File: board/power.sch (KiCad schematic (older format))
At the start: 38 parts, among them U201 ADP3334, U202 ADP3334, U203 LP2985

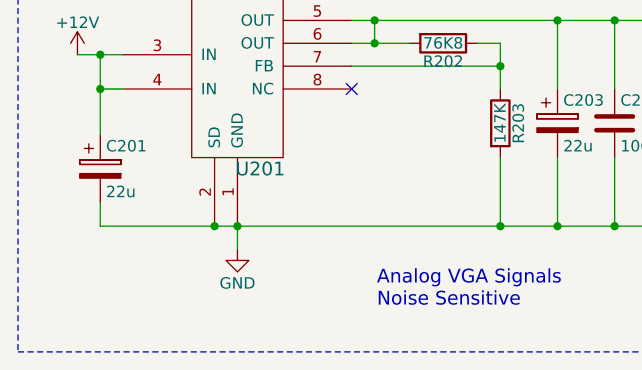
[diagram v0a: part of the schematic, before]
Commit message: Updating netlist.
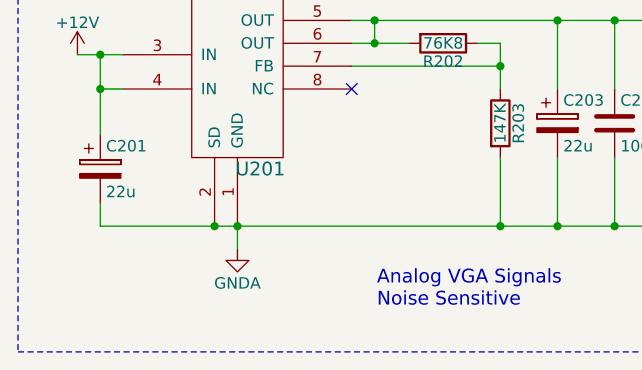
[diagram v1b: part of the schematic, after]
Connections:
- net GND: no longer C201.2, C203.2, C205.2, C207.2, C209.2, C211.2, C213.2, R203.2, R205.2, U201.1 (GND), U201.2 (SD)
- new net GNDA: C201.2, C203.2, C205.2, C207.2, C209.2, C211.2, C213.2, R203.2, R205.2, U201.1 (GND), U201.2 (SD)
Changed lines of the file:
@@
 Connection ~ 2900 4300
 $Comp
-L GND #PWR02
+L GNDA #PWR02
 U 1 1 563F0C8E
 P 2300 5300
 F 0 "#PWR02" H 2300 5050 50  0001 C CNN
-F 1 "GND" H 2300 5150 50  0000 C CNN
+F 1 "GNDA" H 2300 5150 50  0000 C CNN
 F 2 "" H 2300 5300 60  0000 C CNN
 F 3 "" H 2300 5300 60  0000 C CNN

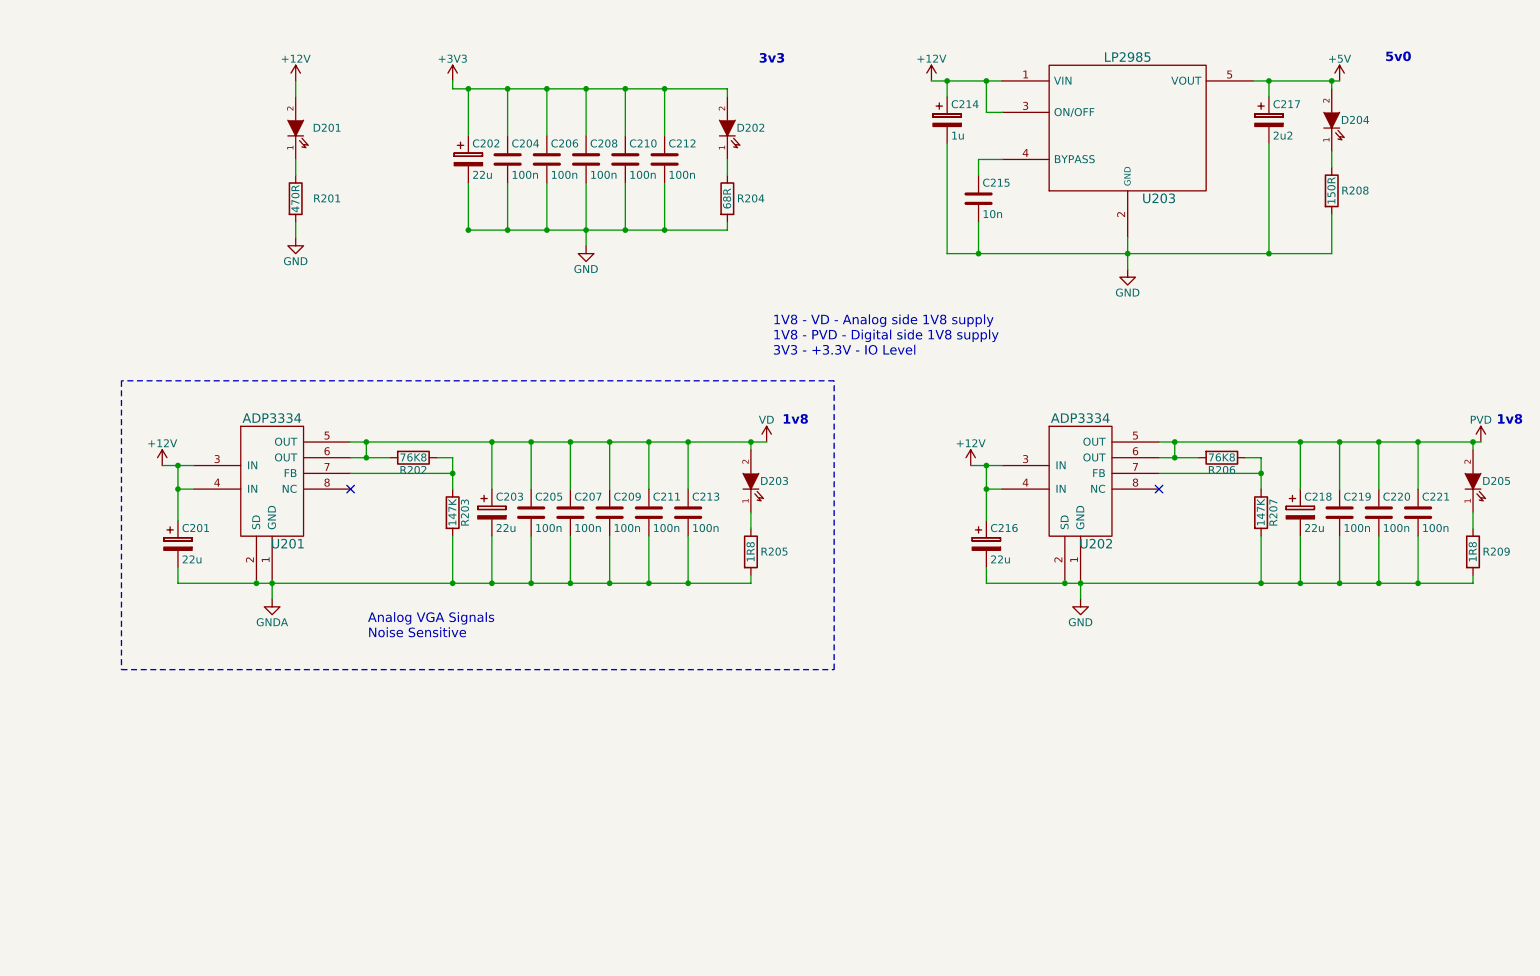
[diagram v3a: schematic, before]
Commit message: Lots of small tweaks.
 * Giving things better reference names.
 * Giving a bunch of nets names.
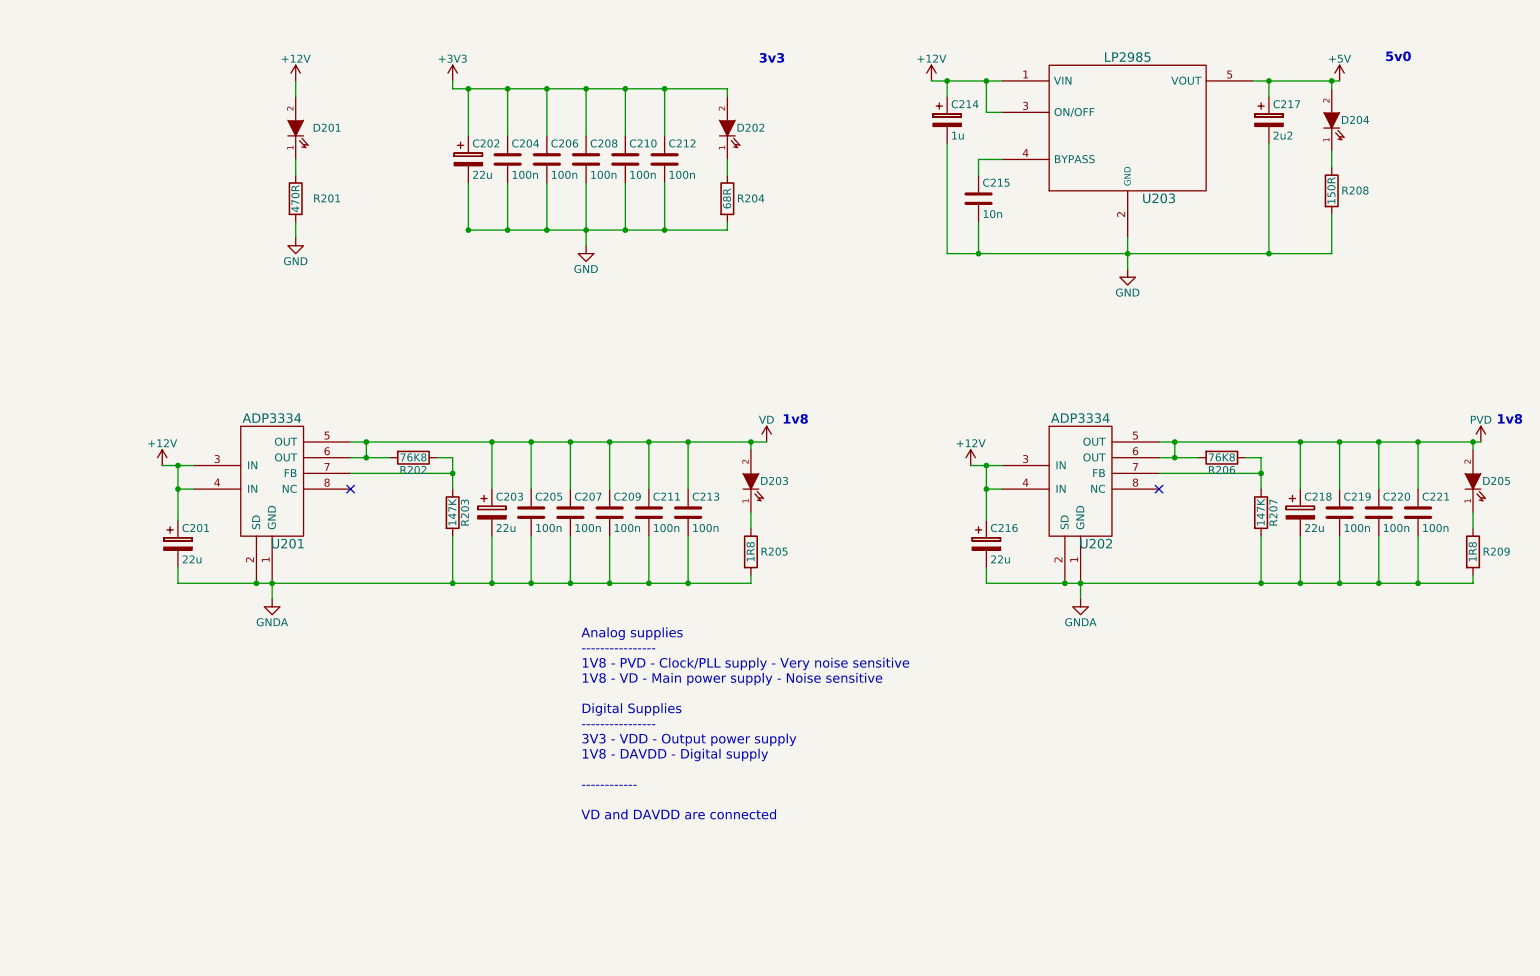
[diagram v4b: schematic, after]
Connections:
- net GND: no longer C216.2, C218.2, C219.2, C220.2, C221.2, R207.2, R209.2, U202.1 (GND), U202.2 (SD)
- net GNDA: now also C216.2, C218.2, C219.2, C220.2, C221.2, R207.2, R209.2, U202.1 (GND), U202.2 (SD)
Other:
- note added: "Analog supplies\n----------------\n1V8 - PVD - Clock/PLL supply - Very noise sensitive\n1V8 - VD - Main power supply - Noise sensitive\n\nDigital Supplies\n----------------\n3V3 - VDD - Output power supply\n1V8 - DAVDD - Digital supply\n\n------------\n\nVD and DAVDD are connected"
- note removed: "1V8 - VD - Analog side 1V8 supply\n1V8 - PVD - Digital side 1V8 supply\n3V3 - +3.3V - IO Level"
- note removed: "Analog VGA Signals\nNoise Sensitive\n"
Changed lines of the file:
@@
 Connection ~ 8050 4300
 $Comp
-L GND #PWR11
+L GNDA #PWR11
 U 1 1 56420FD1
 P 7450 5300
 F 0 "#PWR11" H 7450 5050 50  0001 C CNN
-F 1 "GND" H 7450 5150 50  0000 C CNN
+F 1 "GNDA" H 7450 5150 50  0000 C CNN
 F 2 "" H 7450 5300 60  0000 C CNN
 F 3 "" H 7450 5300 60  0000 C CNN
@@
 Text Notes 9390 1890 0    60   ~ 12
 5v0
-Text Notes 5490 3760 0    60   ~ 0
-1V8 - VD - Analog side 1V8 supply\n1V8 - PVD - Digital side 1V8 supply\n3V3 - +3.3V - IO Level
-Text Notes 2910 5560 0    60   ~ 0
-Analog VGA Signals\nNoise Sensitive\n
-Wire Notes Line
-	1340 3910 1340 5750
-Wire Notes Line
-	1340 5750 5880 5750
-Wire Notes Line
-	5880 5750 5880 3910
-Wire Notes Line
-	5880 3910 1340 3910
+Text Notes 4270 6720 0    60   ~ 0
+Analog supplies\n----------------\n1V8 - PVD - Clock/PLL supply - Very noise sensitive\n1V8 - VD - Main power supply - Noise sensitive\n\nDigital Supplies\n----------------\n3V3 - VDD - Output power supply\n1V8 - DAVDD - Digital supply\n\n------------\n\nVD and DAVDD are connected
 $EndSCHEMATC

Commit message: More and hopefully better labelling.
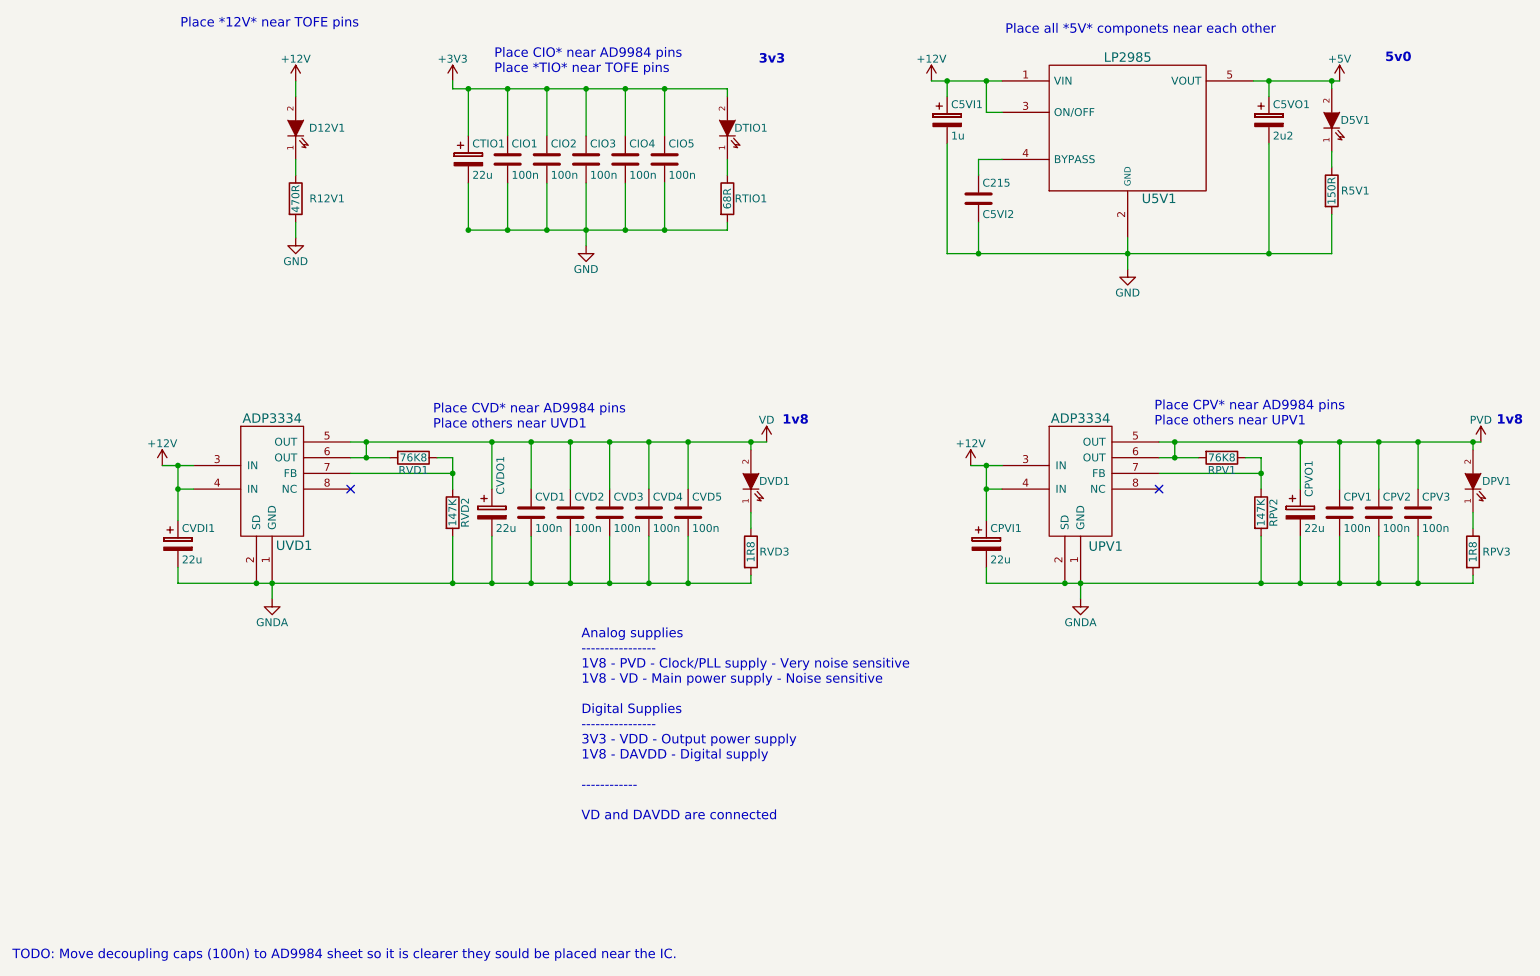
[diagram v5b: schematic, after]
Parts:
- C215: value 10n -> C5VI2
- renumbered C214 to C5VI1, C217 to C5VO1, C204 to CIO1, C206 to CIO2, C208 to CIO3, C210 to CIO4, C212 to CIO5, C219 to CPV1, C220 to CPV2, C221 to CPV3, C216 to CPVI1, C218 to CPVO1, C202 to CTIO1, C205 to CVD1, C207 to CVD2, C209 to CVD3, C211 to CVD4, C213 to CVD5, C201 to CVDI1, C203 to CVDO1, D201 to D12V1, D204 to D5V1, D205 to DPV1, D202 to DTIO1, D203 to DVD1, R201 to R12V1, R208 to R5V1, R206 to RPV1, R207 to RPV2, R209 to RPV3, R204 to RTIO1, R202 to RVD1, R203 to RVD2, R205 to RVD3, U203 to U5V1, U202 to UPV1, U201 to UVD1
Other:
- note added: "Place *12V* near TOFE pins"
- note added: "Place CIO* near AD9984 pins\nPlace *TIO* near TOFE pins"
- note added: "Place CPV* near AD9984 pins\nPlace others near UPV1"
- note added: "Place CVD* near AD9984 pins\nPlace others near UVD1"
- note added: "Place all *5V* componets near each other"
- note added: "TODO: Move decoupling caps (100n) to AD9984 sheet so it is clearer they sould be placed near the IC."

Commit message: Updating net names.
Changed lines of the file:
@@
 $EndDescr
 $Comp
-L GND #PWR02
+L GND #PWR7
 U 1 1 563EFCF4
 P 4300 3050
-F 0 "#PWR02" H 4300 2800 50  0001 C CNN
+F 0 "#PWR7" H 4300 2800 50  0001 C CNN
 F 1 "GND" H 4300 2900 50  0000 C CNN
 F 2 "" H 4300 3050 60  0000 C CNN
@@
 Connection ~ 2900 4300
 $Comp
-L GNDA #PWR03
+L GNDA #PWR3
 U 1 1 563F0C8E
 P 2300 5300
-F 0 "#PWR03" H 2300 5050 50  0001 C CNN
+F 0 "#PWR3" H 2300 5050 50  0001 C CNN
 F 1 "GNDA" H 2300 5150 50  0000 C CNN
 F 2 "" H 2300 5300 60  0000 C CNN
@@
 	2300 5200 2300 5300
 $Comp
-L PVD #PWR04
+L PVD #PWR14
 U 1 1 56411BE9
 P 10000 4300
-F 0 "#PWR04" H 10000 4150 50  0001 C CNN
+F 0 "#PWR14" H 10000 4150 50  0001 C CNN
 F 1 "PVD" H 10000 4440 50  0000 C CNN
 F 2 "" H 10000 4300 60  0000 C CNN
@@
 $EndComp
 $Comp
-L VD #PWR05
+L VD #PWR8
 U 1 1 56411CB5
 P 5450 4300
-F 0 "#PWR05" H 5450 4150 50  0001 C CNN
+F 0 "#PWR8" H 5450 4150 50  0001 C CNN
 F 1 "VD" H 5450 4440 50  0000 C CNN
 F 2 "" H 5450 4300 60  0000 C CNN
@@
 Connection ~ 8050 4300
 $Comp
-L GNDA #PWR06
+L GNDA #PWR11
 U 1 1 56420FD1
 P 7450 5300
-F 0 "#PWR06" H 7450 5050 50  0001 C CNN
+F 0 "#PWR11" H 7450 5050 50  0001 C CNN
 F 1 "GNDA" H 7450 5150 50  0000 C CNN
 F 2 "" H 7450 5300 60  0000 C CNN
@@
 	6850 5200 9950 5200
 $Comp
-L +5V #PWR07
+L +5V #PWR13
 U 1 1 5642563F
 P 9100 2000
-F 0 "#PWR07" H 9100 1850 50  0001 C CNN
+F 0 "#PWR13" H 9100 1850 50  0001 C CNN
 F 1 "+5V" H 9100 2140 50  0000 C CNN
 F 2 "" H 9100 2000 60  0000 C CNN
@@
 $EndComp
 $Comp
-L +12V #PWR08
+L +12V #PWR9
 U 1 1 56426036
 P 6500 2000
-F 0 "#PWR08" H 6500 1850 50  0001 C CNN
+F 0 "#PWR9" H 6500 1850 50  0001 C CNN
 F 1 "+12V" H 6500 2140 50  0000 C CNN
 F 2 "" H 6500 2000 60  0000 C CNN
@@
 Connection ~ 6800 3100
 $Comp
-L GND #PWR09
+L GND #PWR12
 U 1 1 56426AF7
 P 7750 3200
-F 0 "#PWR09" H 7750 2950 50  0001 C CNN
+F 0 "#PWR12" H 7750 2950 50  0001 C CNN
 F 1 "GND" H 7750 3050 50  0000 C CNN
 F 2 "" H 7750 3200 60  0000 C CNN
@@
 $EndComp
 $Comp
-L +12V #PWR010
+L +12V #PWR10
 U 1 1 5642782E
 P 6750 4450
-F 0 "#PWR010" H 6750 4300 50  0001 C CNN
+F 0 "#PWR10" H 6750 4300 50  0001 C CNN
 F 1 "+12V" H 6750 4590 50  0000 C CNN
 F 2 "" H 6750 4450 60  0000 C CNN
@@
 $EndComp
 $Comp
-L +12V #PWR011
+L +12V #PWR2
 U 1 1 5642787C
 P 1600 4450
-F 0 "#PWR011" H 1600 4300 50  0001 C CNN
+F 0 "#PWR2" H 1600 4300 50  0001 C CNN
 F 1 "+12V" H 1600 4590 50  0000 C CNN
 F 2 "" H 1600 4450 60  0000 C CNN
@@
 $EndComp
 $Comp
-L +3V3 #PWR012
+L +3V3 #PWR6
 U 1 1 56924AD1
 P 3450 2000
-F 0 "#PWR012" H 3450 1850 50  0001 C CNN
+F 0 "#PWR6" H 3450 1850 50  0001 C CNN
 F 1 "+3V3" H 3450 2140 50  0000 C CNN
 F 2 "" H 3450 2000 50  0000 C CNN
@@
 $EndComp
 $Comp
-L +12V #PWR013
+L +12V #PWR4
 U 1 1 56924BE7
 P 2450 2000
-F 0 "#PWR013" H 2450 1850 50  0001 C CNN
+F 0 "#PWR4" H 2450 1850 50  0001 C CNN
 F 1 "+12V" H 2450 2140 50  0000 C CNN
 F 2 "" H 2450 2000 50  0000 C CNN
@@
 $EndComp
 $Comp
-L GND #PWR014
+L GND #PWR5
 U 1 1 56925059
 P 2450 3000
-F 0 "#PWR014" H 2450 2750 50  0001 C CNN
+F 0 "#PWR5" H 2450 2750 50  0001 C CNN
 F 1 "GND" H 2450 2850 50  0000 C CNN
 F 2 "" H 2450 3000 50  0000 C CNN
@@
 Text Notes 645  7605 0    60   ~ 0
 TODO: Move decoupling caps (100n) to AD9984 sheet so it is clearer they sould be placed near the IC.
+Text Label 4900 2050 0    60   ~ 0
+VCC3V3
+Text Label 2450 2050 0    60   ~ 0
+VCC12V
+Text Label 6650 2000 0    60   ~ 0
+VCC12V
+Text Label 6850 4800 1    60   ~ 0
+VCC12V
+Text Label 1700 4800 1    60   ~ 0
+VCC12V
+Text Label 8650 2000 0    60   ~ 0
+VCC5V0
+Text Label 9100 4300 0    60   ~ 0
+PVD
+Text Label 4950 4300 0    60   ~ 0
+VD
 $EndSCHEMATC

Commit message: Moving I2C enable pins to make IO1 a NC.
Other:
- note added: "Place 1v8 supplies (UPV1 and UVD1) as close to \nthe AD9938 as possible without introducing noise."
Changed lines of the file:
@@
 Text Label 4950 4300 0    60   ~ 0
 VD
+Text Notes 4900 3670 0    60   ~ 0
+Place 1v8 supplies (UPV1 and UVD1) as close to \nthe AD9938 as possible without introducing noise.
 $EndSCHEMATC
